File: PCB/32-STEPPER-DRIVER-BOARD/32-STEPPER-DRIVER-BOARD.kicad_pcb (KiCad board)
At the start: 2 copper layers, 100 x 100 mm, 412 parts, among them J1 MEC2-30-01-X-TH1-NP-WT, J2 MEC2-30-01-X-TH1-NP-WT, J3 MEC2-30-01-X-TH1-NP-WT, J4 MEC2-30-01-X-TH1-NP-WT, U1 74HC595, U10 74HC595, U11 74HC595, U12 74HC595, U13 74HC595, U14 74HC595, U15 74HC595, U16 74HC595, U17 74HC595, U18 74HC595, U19 74HC595, U2 74HC595, U20 74HC595, U21 74HC595, U22 74HC595, U23 74HC595, U24 74HC595, U3 74HC595, U4 74HC595, U5 74HC595, U6 74HC595, U7 74HC595, U8 74HC595, U9 74HC595

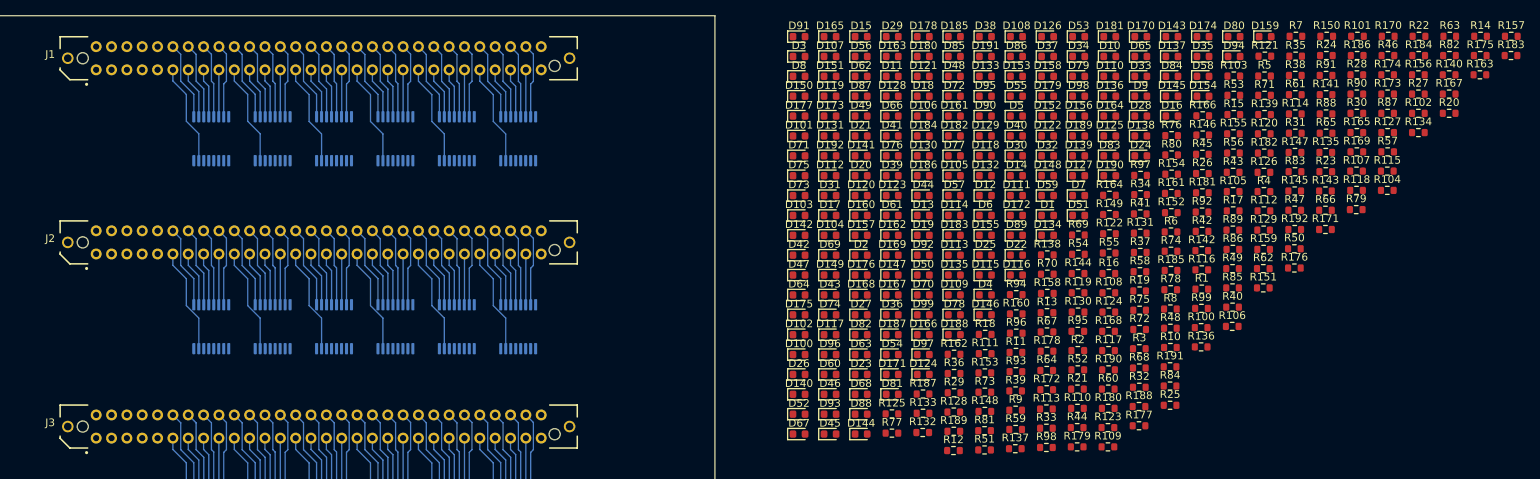
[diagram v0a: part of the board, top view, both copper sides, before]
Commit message: MORE 32-STEPPER LAYOUT WORK
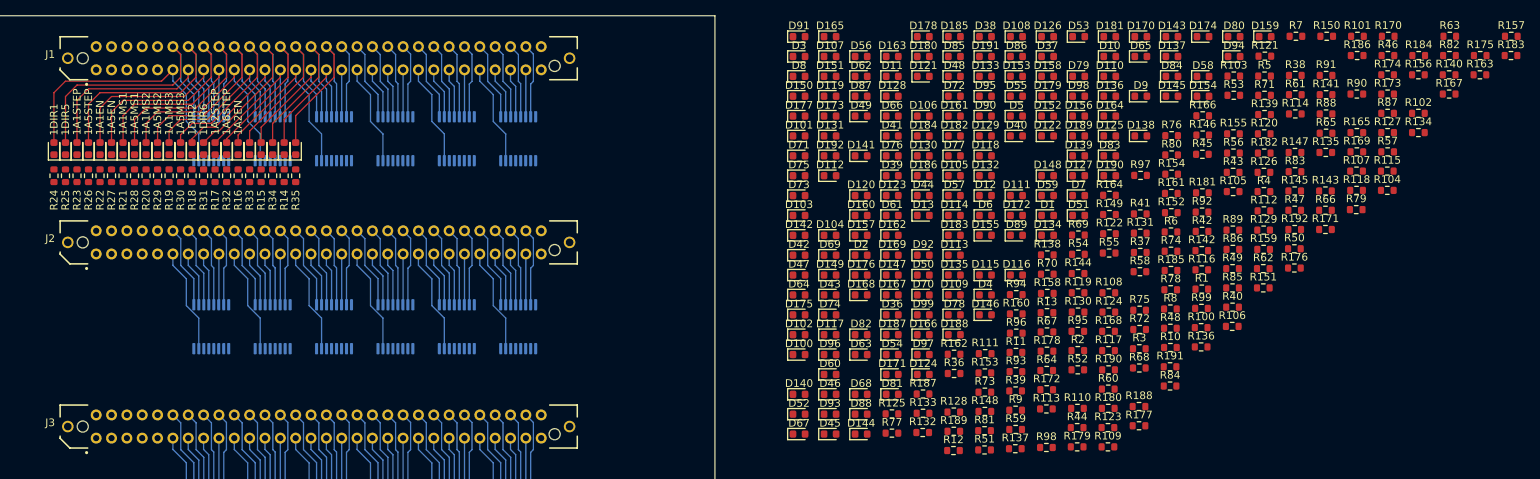
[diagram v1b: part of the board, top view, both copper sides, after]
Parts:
- moved R22 172.9 mm to (60.5, 34.8), turned to -90 degrees
- moved R27 170.7 mm to (62.0, 34.8), turned to -90 degrees
- moved R20 170.0 mm to (66.5, 34.8), turned to -90 degrees
- moved R24 166.6 mm to (54.5, 34.8), turned to -90 degrees
- moved R23 162.8 mm to (57.5, 34.8), turned to -90 degrees
- moved R28 159.8 mm to (65.0, 34.8), turned to -90 degrees
- moved R14 157.0 mm to (84.5, 34.8), turned to -90 degrees
- moved R30 153.5 mm to (71.0, 34.8), turned to -90 degrees
- moved R25 147.0 mm to (56.0, 34.8), turned to -90 degrees
- moved R26 145.2 mm to (59.0, 34.8), turned to -90 degrees
- moved R31 142.4 mm to (74.0, 34.8), turned to -90 degrees
- moved D24 141.7 mm to (54.5, 31.3), turned to 90 degrees
- moved R17 132.8 mm to (75.5, 34.8), turned to -90 degrees
- moved R35 131.2 mm to (86.0, 34.8), turned to -90 degrees
- moved D28 131.2 mm to (65.0, 31.3), turned to 90 degrees
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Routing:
- net 1DIR5: track 10.3 -> 36.7 mm
- net 1A5STEP: track 9.98 -> 34.8 mm
- net 1A5EN: track 9.69 -> 32.9 mm
- net 1DIR1: track 13.2 -> 36.5 mm
- net 1A1STEP: track 6.69 -> 28.9 mm
- net 1A5MS1: track 9.69 -> 31.4 mm
- net 1A1EN: track 6.40 -> 27.0 mm
- net 1A5MS2: track 10.3 -> 30.4 mm
- net 1A1MS1: track 6.13 -> 25.2 mm
- net 1A5MS3: track 9.98 -> 28.5 mm
- net 1A1MS2: track 13.2 -> 30.7 mm
- net 1DIR6: track 9.69 -> 26.6 mm
- net 1A6STEP: track 9.69 -> 25.9 mm
- net 1A1MS3: track 6.69 -> 22.6 mm
- net 1A6EN: track 10.3 -> 26.1 mm
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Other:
- board text added: "1A1EN"
- board text added: "1A1MS1"
- board text added: "1A1MS2"
- board text added: "1A1MS3"
- board text added: "1A1STEP"
- board text added: "1A2EN"
- board text added: "1A2STEP"
- board text added: "1A5EN"
- board text added: "1A5MS1"
- board text added: "1A5MS2"
- board text added: "1A5MS3"
- board text added: "1A5STEP"
- board text added: "1A6STEP"
- board text added: "1DIR1"
- board text added: "1DIR2"
- board text added: "1DIR5"
- board text added: "1DIR6"

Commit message: progress
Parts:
- moved R38 122.0 mm to (95.0, 34.8), turned to -90 degrees
- moved R7 112.3 mm to (105.5, 34.8), turned to -90 degrees
- moved R46 110.5 mm to (119.0, 34.8), turned to -90 degrees
- moved R40 108.5 mm to (101.0, 34.8), turned to -90 degrees
- moved R10 105.9 mm to (96.5, 34.8), turned to -90 degrees
- moved R37 104.6 mm to (92.0, 34.8), turned to -90 degrees
- moved R5 101.6 mm to (111.5, 34.8), turned to -90 degrees
- moved R8 99.0 mm to (102.5, 34.8), turned to -90 degrees
- moved R43 98.2 mm to (110.0, 34.8), turned to -90 degrees
- moved R13 98.1 mm to (87.5, 34.8), turned to -90 degrees
- moved R4 97.7 mm to (114.5, 34.8), turned to -90 degrees
- moved R42 97.4 mm to (107.0, 34.8), turned to -90 degrees
- moved D9 96.9 mm to (99.5, 31.3), turned to 90 degrees
- moved D10 96.4 mm to (96.5, 31.3), turned to 90 degrees
- moved R47 94.3 mm to (122.0, 34.8), turned to -90 degrees
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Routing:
- net ~{SRCLR}: track 0.00 -> 126.1 mm
- net SRCLK: track 0.00 -> 119.7 mm
- net RCLK: track 0.00 -> 119.1 mm
- net ~{OE}: track 0.00 -> 112.5 mm
- net GND: track 0.00 -> 70.5 mm
- net +5V: track 0.00 -> 20.5 mm
- net 1A8MS3: track 9.69 -> 25.9 mm
- net 1A8MS2: track 9.69 -> 25.5 mm
- net 1A8MS1: track 9.98 -> 25.4 mm
- net 1A8EN: track 10.3 -> 25.3 mm
- net 1A8STEP: track 9.69 -> 24.3 mm
- net 1A6MS3: track 9.69 -> 24.3 mm
- net 1DIR7: track 10.3 -> 24.4 mm
- net 1DIR8: track 9.69 -> 23.8 mm
- net 1A7STEP: track 9.98 -> 23.7 mm
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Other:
- board text added: "1A2MS1"
- board text added: "1A2MS2"
- board text added: "1A2MS3"
- board text added: "1A3EN"
- board text added: "1A3MS1"
- board text added: "1A3MS2"
- board text added: "1A3MS3"
- board text added: "1A3STEP"
- board text added: "1A4EN"
- board text added: "1A4MS1"
- board text added: "1A4MS2"
- board text added: "1A4MS3"
- board text added: "1A4STEP"
- board text added: "1A6EN"
- board text added: "1A6MS1"
- board text added: "1A6MS2"
- board text added: "1A6MS3"
- board text added: "1A7EN"
- board text added: "1A7MS1"
- board text added: "1A7MS2"
- board text added: "1A7MS3"
- board text added: "1A7STEP"
- board text added: "1A8EN"
- board text added: "1A8MS1"
- board text added: "1A8MS2"
- board text added: "1A8MS3"
- board text added: "1A8STEP"
- board text added: "1DIR3"
- board text added: "1DIR4"
- board text added: "1DIR7"
- board text added: "1DIR8"

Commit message: progress
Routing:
- net GND: track 70.5 -> 282.0 mm
- net ~{OE}: track 112.5 -> 144.4 mm, vias 0 -> 6
- net 2DIR5: track 10.3 -> 36.7 mm
- net 4DIR5: track 10.3 -> 36.7 mm
- net 3DIR5: track 10.3 -> 36.7 mm
- net 4A5STEP: track 9.98 -> 34.8 mm
- net 3A5STEP: track 9.98 -> 34.8 mm
- net 2A5STEP: track 9.98 -> 34.8 mm
- net Net-(U5-Pad9): track 0.00 -> 24.8 mm, vias 0 -> 2
- net RCLK: track 119.1 -> 142.4 mm, vias 0 -> 6
- net 4A5EN: track 9.69 -> 32.9 mm
- net 3A5EN: track 9.69 -> 32.9 mm
- net 2A5EN: track 9.69 -> 32.9 mm
- net 4DIR1: track 13.2 -> 36.5 mm
- net 3DIR1: track 13.2 -> 36.5 mm
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
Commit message: progress
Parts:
- moved D100 94.2 mm to (187.0, 145.5)
- moved D101 94.2 mm to (187.0, 117.0)
- moved D102 94.2 mm to (187.0, 142.9)
- moved D103 94.2 mm to (187.0, 127.3)
- moved D105 94.2 mm to (207.2, 122.2)
- moved D108 94.2 mm to (215.3, 104.0)
- moved D111 94.2 mm to (215.3, 124.8)
- moved D113 94.2 mm to (207.2, 132.5)
- moved D114 94.2 mm to (207.2, 127.3)
- moved D116 94.2 mm to (215.3, 135.1)
- moved D120 94.2 mm to (195.1, 124.8)
- moved D122 94.2 mm to (219.4, 117.0)
- moved D123 94.2 mm to (199.1, 124.8)
- moved D125 94.2 mm to (227.5, 117.0)
- moved D126 94.2 mm to (219.4, 104.0)
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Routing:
- net GND: track 282.0 -> 414.1 mm
- net +5V: track 10.3 -> 95.6 mm, vias 0 -> 6
- net ~{SRCLR}: track 135.4 -> 72.3 mm
- net SRCLK: track 137.6 -> 77.7 mm
- net RCLK: track 142.4 -> 82.8 mm
- net ~{OE}: track 144.4 -> 88.2 mm
- net Net-(U4-Pad9): track 0.00 -> 26.1 mm, vias 0 -> 2
- net Net-(U4-Pad14): track 0.00 -> 26.1 mm, vias 0 -> 2
- net Net-(U3-Pad14): track 0.00 -> 26.1 mm, vias 0 -> 2
- net Net-(U2-Pad14): track 0.00 -> 26.1 mm, vias 0 -> 2
- net 2DIR1: track 39.6 -> 23.2 mm
- net 1DIR3: track 10.9 -> 24.2 mm
- net 1A4EN: track 11.3 -> 24.6 mm
- net 1A2EN: track 12.6 -> 25.8 mm
- net 1A1MS2: track 17.5 -> 30.7 mm
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
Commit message: added more connectors
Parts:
- removed D101, D107, D11, D113, D119, D122, D128, D134, D140, D149, D155, D161, D167, D17, D173, D179, D185, D191, D23, D26, D32, D38, D44, D5, D53, D59, D65, D71, D74, D80, D86, D92: LED, LED_SMD:LED_0603_1608Metric
- removed R101, R107, R11, R113, R119, R122, R128, R134, R140, R149, R155, R161, R167, R17, R173, R179, R185, R191, R23, R26, R32, R38, R44, R5, R53, R59, R65, R71, R74, R80, R86, R92: R, Resistor_SMD:R_0603_1608Metric
- removed U16, U23, U24, U8: 74HC595, Package_SO:TSSOP-16_4.4x5mm_P0.65mm
- added J5: IPS1-125-01-S-D, LIBRARIES:SAMTEC_IPS1-125-01-S-D, F.Cu at (135.7, 64.0)
- added J6: UMPT-06-01-X-RA-WT-P-X, LIBRARIES:SAMTEC_UMPT-06-01-X-RA-WT-P-X, B.Cu at (44.0, 85.0)
- moved D24 9.30 mm to (63.8, 31.3)
- moved D25 9.30 mm to (65.3, 31.3)
- moved R24 9.30 mm to (63.8, 34.8)
- moved R25 9.30 mm to (65.3, 34.8)
- moved D18 6.30 mm to (78.8, 31.3)
- moved D19 6.30 mm to (75.8, 31.3)
- moved D20 6.30 mm to (72.8, 31.3)
- moved D21 6.30 mm to (69.8, 31.3)
- moved D22 6.30 mm to (66.8, 31.3)
- moved D27 6.30 mm to (68.3, 31.3)
- moved D28 6.30 mm to (71.3, 31.3)
- moved D29 6.30 mm to (74.3, 31.3)
- moved D30 6.30 mm to (77.3, 31.3)
- moved D31 6.30 mm to (80.3, 31.3)
- moved R18 6.30 mm to (78.8, 34.8)
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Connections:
- D169 pad 2: 4A4MS3 -> 4DIR5
- D170 pad 2: 4A4MS2 -> 4A8MS1
- D171 pad 2: 4A4MS1 -> 4A8MS2
- D172 pad 2: 4A4EN -> 4A8MS3
- D174 pad 2: 4DIR4 -> 4A5EN
- D175 pad 2: 4A3MS3 -> 4A5MS1
- D176 pad 2: 4A3MS2 -> 4A5MS2
- D177 pad 2: 4A3MS1 -> 4A5MS3
- D178 pad 2: 4A3EN -> 4DIR6
- D180 pad 2: 4DIR3 -> 4A6EN
- D181 pad 2: 4A2MS3 -> 4A6MS1
- D182 pad 2: 4A2MS2 -> 4A6MS2
- D183 pad 2: 4A2MS1 -> 4A6MS3
- D184 pad 2: 4A2EN -> 4DIR7
- D186 pad 2: 4DIR2 -> 4A7EN
- D187 pad 2: 4A1MS3 -> 4A7MS1
- D188 pad 2: 4A1MS2 -> 4A7MS2
- D189 pad 2: 4A1MS1 -> 4A7MS3
- D190 pad 2: 4A1EN -> 4DIR8
- D192 pad 2: 4DIR1 -> 4A8EN
- U10 pad 1: 2A6EN -> 2A6MS2
- U10 pad 15: 2A2EN -> 2A2MS2
- U10 pad 2: 2A2MS1 -> 2A2MS3
- U10 pad 3: 2A6MS1 -> 2A6MS3
- U10 pad 4: 2A2MS2 -> 2A1MS2
- U10 pad 5: 2A6MS2 -> 2A5MS2
- U10 pad 6: 2A2MS3 -> 2A1MS3
- U10 pad 7: 2A6MS3 -> 2A5MS3
- U11 pad 1: 2A5MS2 -> 2DIR6
- U11 pad 15: 2A1MS2 -> 2DIR2
- U11 pad 2: 2A1MS3 -> 2DIR1
- U11 pad 3: 2A5MS3 -> 2DIR5
- U11 pad 4: 2DIR2 -> 2A1EN
- U11 pad 5: 2DIR6 -> 2A5EN
- U11 pad 6: 2A2STEP -> 2A1MS1
- U11 pad 7: 2A6STEP -> 2A5MS1
- U11 pad 9: Net-(U12-Pad14) -> unconnected-(U11-Pad9)
- U12 pad 1: 2DIR5 -> 3A8EN
- U12 pad 14: Net-(U12-Pad14) -> SER3
- U12 pad 15: 2DIR1 -> 3A4EN
- U12 pad 2: 2A1STEP -> 3A4MS1
- U12 pad 3: 2A5STEP -> 3A8MS1
- U12 pad 4: 2A1EN -> 3A4MS2
- U12 pad 5: 2A5EN -> 3A8MS2
- U12 pad 6: 2A1MS1 -> 3A4MS3
- U12 pad 7: 2A5MS1 -> 3A8MS3
- U13 pad 1: 3A8EN -> 3A7MS2
- U13 pad 15: 3A4EN -> 3A3MS2
- U13 pad 2: 3A4MS1 -> 3A3MS3
- U13 pad 3: 3A8MS1 -> 3A7MS3
- U13 pad 4: 3A4MS2 -> 3DIR4
- U13 pad 5: 3A8MS2 -> 3DIR8
- U13 pad 6: 3A4MS3 -> 3DIR3
- U13 pad 7: 3A8MS3 -> 3DIR7
- U14 pad 1: 3A7MS2 -> 3A7EN
- U14 pad 15: 3A3MS2 -> 3A3EN
- U14 pad 2: 3A3MS3 -> 3A3MS1
- U14 pad 3: 3A7MS3 -> 3A7MS1
- U14 pad 4: 3DIR4 -> 3A1MS2
- U14 pad 5: 3DIR8 -> 3A5MS2
- U14 pad 6: 3A4STEP -> 3A1MS3
- U14 pad 7: 3A8STEP -> 3A5MS3
- U15 pad 1: 3DIR7 -> 3DIR6
- U15 pad 15: 3DIR3 -> 3DIR2
- U15 pad 2: 3A3STEP -> 3DIR1
- U15 pad 3: 3A7STEP -> 3DIR5
- U15 pad 4: 3A3EN -> 3A1EN
- U15 pad 5: 3A7EN -> 3A5EN
- U15 pad 6: 3A3MS1 -> 3A1MS1
- U15 pad 7: 3A7MS1 -> 3A5MS1
- U15 pad 9: Net-(U15-Pad9) -> unconnected-(U15-Pad9)
- U17 pad 1: 3A5MS2 -> 3A6EN
- U17 pad 14: SER3 -> unconnected-(U17-Pad14)
- U17 pad 15: 3A1MS2 -> 3A2EN
- U17 pad 2: 3A1MS3 -> 3A2MS1
- U17 pad 3: 3A5MS3 -> 3A6MS1
- U17 pad 4: 3DIR2 -> 3A2MS2
- U17 pad 5: 3DIR6 -> 3A6MS2
- U17 pad 6: 3A2STEP -> 3A2MS3
- U17 pad 7: 3A6STEP -> 3A6MS3
- U17 pad 9: Net-(U18-Pad14) -> unconnected-(U17-Pad9)
- U18 pad 1: 3DIR5 -> 4A8EN
- U18 pad 14: Net-(U18-Pad14) -> SER4
- U18 pad 15: 3DIR1 -> 4A4EN
- U18 pad 2: 3A1STEP -> 4A4MS1
- U18 pad 3: 3A5STEP -> 4A8MS1
- U18 pad 4: 3A1EN -> 4A4MS2
- U18 pad 5: 3A5EN -> 4A8MS2
- U18 pad 6: 3A1MS1 -> 4A4MS3
- U18 pad 7: 3A5MS1 -> 4A8MS3
- U19 pad 1: 4A8EN -> 4A7MS2
- U19 pad 15: 4A4EN -> 4A3MS2
- U19 pad 2: 4A4MS1 -> 4A3MS3
- U19 pad 3: 4A8MS1 -> 4A7MS3
- U19 pad 4: 4A4MS2 -> 4DIR4
- U19 pad 5: 4A8MS2 -> 4DIR8
- U19 pad 6: 4A4MS3 -> 4DIR3
- U19 pad 7: 4A8MS3 -> 4DIR7
- U2 pad 6: 1A4STEP -> 1DIR3
- U2 pad 7: 1A8STEP -> 1DIR7
- U20 pad 1: 4A7MS2 -> 4A7EN
- U20 pad 15: 4A3MS2 -> 4A3EN
- U20 pad 2: 4A3MS3 -> 4A3MS1
- U20 pad 3: 4A7MS3 -> 4A7MS1
- U20 pad 4: 4DIR4 -> 4A2EN
- U20 pad 5: 4DIR8 -> 4A6EN
- U20 pad 6: 4A4STEP -> 4A2MS1
- U20 pad 7: 4A8STEP -> 4A6MS1
- U21 pad 1: 4DIR7 -> 4A6MS2
- U21 pad 15: 4DIR3 -> 4A2MS2
- U21 pad 2: 4A3STEP -> 4A2MS3
- U21 pad 3: 4A7STEP -> 4A6MS3
- U21 pad 4: 4A3EN -> 4A1MS2
- U21 pad 5: 4A7EN -> 4A5MS2
- U21 pad 6: 4A3MS1 -> 4A1MS3
- U21 pad 7: 4A7MS1 -> 4A5MS3
- U22 pad 1: 4A6EN -> 4DIR6
- U22 pad 15: 4A2EN -> 4DIR2
- U22 pad 2: 4A2MS1 -> 4DIR1
- U22 pad 3: 4A6MS1 -> 4DIR5
- U22 pad 4: 4A2MS2 -> 4A1EN
- U22 pad 5: 4A6MS2 -> 4A5EN
- U22 pad 6: 4A2MS3 -> 4A1MS1
- U22 pad 7: 4A6MS3 -> 4A5MS1
- U22 pad 9: Net-(U22-Pad9) -> unconnected-(U22-Pad9)
- U3 pad 1: 1DIR7 -> 1A7EN
- U3 pad 15: 1DIR3 -> 1A3EN
- U3 pad 2: 1A3STEP -> 1A3MS1
- U3 pad 3: 1A7STEP -> 1A7MS1
- U3 pad 4: 1A3EN -> 1A2EN
- U3 pad 5: 1A7EN -> 1A6EN
- U3 pad 6: 1A3MS1 -> 1A2MS1
- U3 pad 7: 1A7MS1 -> 1A6MS1
- U4 pad 1: 1A6EN -> 1A6MS2
- U4 pad 15: 1A2EN -> 1A2MS2
- U4 pad 2: 1A2MS1 -> 1A2MS3
- U4 pad 3: 1A6MS1 -> 1A6MS3
- U4 pad 4: 1A2MS2 -> 1A1MS2
- U4 pad 5: 1A6MS2 -> 1A5MS2
- U4 pad 6: 1A2MS3 -> 1A1MS3
- U4 pad 7: 1A6MS3 -> 1A5MS3
- U5 pad 1: 1A5MS2 -> 1DIR6
- U5 pad 15: 1A1MS2 -> 1DIR2
- U5 pad 2: 1A1MS3 -> 1DIR1
- U5 pad 3: 1A5MS3 -> 1DIR5
- U5 pad 4: 1DIR2 -> 1A1EN
- U5 pad 5: 1DIR6 -> 1A5EN
- U5 pad 6: 1A2STEP -> 1A1MS1
- U5 pad 7: 1A6STEP -> 1A5MS1
- U5 pad 9: Net-(U5-Pad9) -> unconnected-(U5-Pad9)
- U6 pad 1: 1DIR5 -> 2A8EN
- U6 pad 14: Net-(U5-Pad9) -> SER2
- U6 pad 15: 1DIR1 -> 2A4EN
- U6 pad 2: 1A1STEP -> 2A4MS1
- U6 pad 3: 1A5STEP -> 2A8MS1
- U6 pad 4: 1A1EN -> 2A4MS2
- U6 pad 5: 1A5EN -> 2A8MS2
- U6 pad 6: 1A1MS1 -> 2A4MS3
- U6 pad 7: 1A5MS1 -> 2A8MS3
- U7 pad 1: 2A8EN -> 2A7MS2
- U7 pad 15: 2A4EN -> 2A3MS2
- U7 pad 2: 2A4MS1 -> 2A3MS3
- U7 pad 3: 2A8MS1 -> 2A7MS3
- U7 pad 4: 2A4MS2 -> 2DIR4
- U7 pad 5: 2A8MS2 -> 2DIR8
- U7 pad 6: 2A4MS3 -> 2DIR3
- U7 pad 7: 2A8MS3 -> 2DIR7
- U9 pad 1: 2DIR7 -> 2A7EN
- U9 pad 14: SER2 -> Net-(U7-Pad9)
- U9 pad 15: 2DIR3 -> 2A3EN
- U9 pad 2: 2A3STEP -> 2A3MS1
- U9 pad 3: 2A7STEP -> 2A7MS1
- U9 pad 4: 2A3EN -> 2A2EN
- U9 pad 5: 2A7EN -> 2A6EN
- U9 pad 6: 2A3MS1 -> 2A2MS1
- U9 pad 7: 2A7MS1 -> 2A6MS1
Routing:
- net GND: track 414.1 -> 132.1 mm
- net +5V: track 95.6 -> 246.2 mm
- net ~{OE}: track 88.2 -> 238.1 mm
- net RCLK: track 82.8 -> 231.2 mm
- net SRCLK: track 77.7 -> 225.3 mm
- net ~{SRCLR}: track 72.3 -> 218.5 mm
- net SER2: track 0.00 -> 56.1 mm, vias 0 -> 2
- net 1A1STEP: track 28.9 -> 80.5 mm
- net 1A7MS1: track 22.6 -> 71.9 mm
- net 1DIR7: track 24.4 -> 72.2 mm
- net 1A2STEP: track 19.1 -> 65.6 mm
- net 1A8MS3: track 25.9 -> 70.2 mm
- net 1A5STEP: track 34.8 -> 78.9 mm
- net 1A8MS2: track 25.5 -> 68.5 mm
- net 1A8MS1: track 25.4 -> 67.2 mm
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- added copper zone on B.Cu, net VCC
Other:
- copper layers 2 -> 4

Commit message: progress
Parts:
- moved R118 196.8 mm to (66.8, 84.8), turned to -90 degrees
- moved R63 192.1 mm to (84.8, 59.9), turned to -90 degrees
- moved R79 191.3 mm to (80.3, 59.9), turned to -90 degrees
- moved R82 191.2 mm to (86.3, 59.9), turned to -90 degrees
- moved R66 189.0 mm to (78.8, 59.9), turned to -90 degrees
- moved R72 186.7 mm to (63.8, 59.9), turned to -90 degrees
- moved R120 186.5 mm to (63.8, 84.8), turned to -90 degrees
- moved R121 183.7 mm to (65.3, 84.8), turned to -90 degrees
- moved R75 181.5 mm to (68.3, 59.9), turned to -90 degrees
- moved R68 181.0 mm to (72.8, 59.9), turned to -90 degrees
- moved R62 176.1 mm to (87.8, 59.9), turned to -90 degrees
- moved R78 175.9 mm to (77.3, 59.9), turned to -90 degrees
- moved R57 174.2 mm to (99.8, 59.9), turned to -90 degrees
- moved R87 174.0 mm to (98.3, 59.9), turned to -90 degrees
- moved R76 173.8 mm to (71.3, 59.9), turned to -90 degrees
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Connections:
- J5 pad 17: unconnected-(J5-Pad17) -> 3A4STEP
- J5 pad 18: unconnected-(J5-Pad18) -> 3A8STEP
- J5 pad 19: unconnected-(J5-Pad19) -> 3A3STEP
- J5 pad 20: unconnected-(J5-Pad20) -> 3A7STEP
- J5 pad 21: unconnected-(J5-Pad21) -> 3A2STEP
- J5 pad 22: unconnected-(J5-Pad22) -> 3A6STEP
- J5 pad 23: unconnected-(J5-Pad23) -> 3A1STEP
- J5 pad 24: unconnected-(J5-Pad24) -> 3A5STEP
- J5 pad 25: unconnected-(J5-Pad25) -> 4A4STEP
- J5 pad 26: unconnected-(J5-Pad26) -> 4A8STEP
- J5 pad 27: unconnected-(J5-Pad27) -> 4A3STEP
- J5 pad 28: unconnected-(J5-Pad28) -> 4A7STEP
- J5 pad 29: unconnected-(J5-Pad29) -> 4A2STEP
- J5 pad 30: unconnected-(J5-Pad30) -> 4A6STEP
- J5 pad 31: unconnected-(J5-Pad31) -> 4A1STEP
- J5 pad 32: unconnected-(J5-Pad32) -> 4A5STEP
- U12 pad 4: 3A4MS2 -> 2A1EN
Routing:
- net 4A1STEP: track 6.69 -> 107.4 mm
- net 4A5STEP: track 9.98 -> 109.6 mm
- net 4A2STEP: track 6.13 -> 93.6 mm
- net 2A5STEP: track 0.00 -> 87.4 mm
- net 4A6STEP: track 9.69 -> 95.7 mm
- net 2A1STEP: track 0.00 -> 85.5 mm
- net 3A1STEP: track 0.00 -> 82.6 mm
- net 4A7STEP: track 0.00 -> 81.7 mm
- net 3A5STEP: track 0.00 -> 81.4 mm
- net 4A3STEP: track 0.00 -> 80.1 mm
- net 2A6STEP: track 0.00 -> 72.4 mm
- net 2A2STEP: track 0.00 -> 70.3 mm
- net 3A2STEP: track 0.00 -> 68.0 mm
- net 3A6STEP: track 0.00 -> 66.6 mm
- net 4A4STEP: track 0.00 -> 60.3 mm
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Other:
- board text added: "2DIR1"
- board text removed: "1A1STEP"
- board text removed: "1A2STEP"
- board text removed: "1A3STEP"
- board text removed: "1A4STEP"
- board text removed: "1A5STEP"
- board text removed: "1A6STEP"
- board text removed: "1A7STEP"
- board text removed: "1A8STEP"
